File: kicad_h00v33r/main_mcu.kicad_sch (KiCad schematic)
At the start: 1 part, among them U1 STM32H723ZGT6

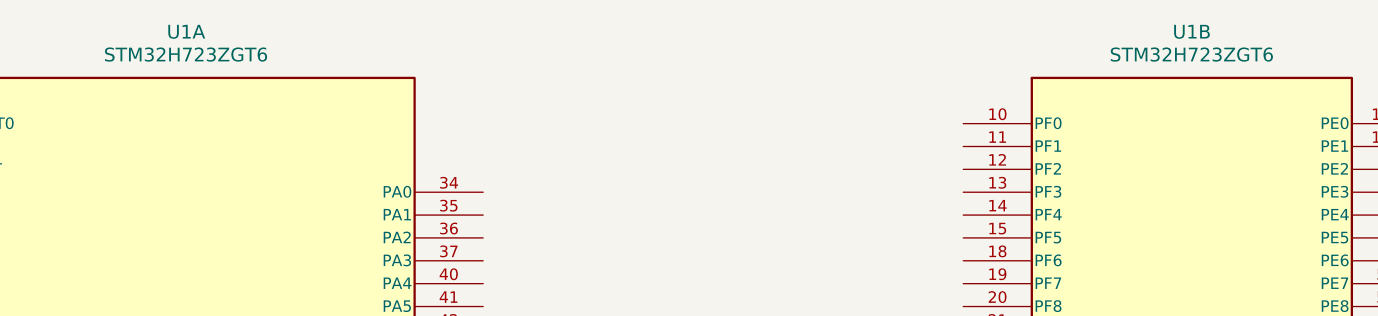
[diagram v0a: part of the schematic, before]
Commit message: power supply + HSE completed
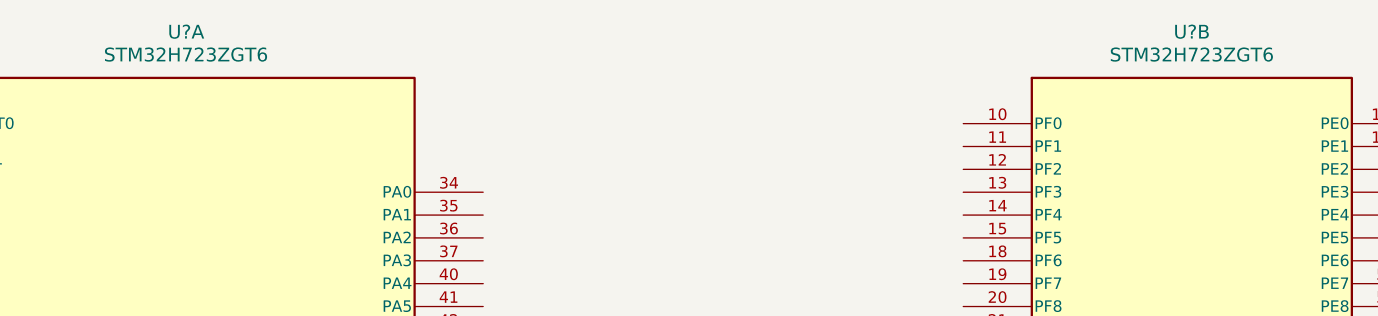
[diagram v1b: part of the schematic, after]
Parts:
- renumbered U1 to U?
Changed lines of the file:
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@@
 		(dnp no)
 		(fields_autoplaced yes)
-		(property "Reference" "U1"
+		(property "Reference" "U?"
 			(at 193.04 45.72 0)
 			(effects
@@
 			(project "kicad_h00v33r"
 				(path "/eacc50d8-8f37-499c-bdc5-63fc65cec568/4cfed190-db6f-4bff-b92a-b36a3b515167"
-					(reference "U1")
+					(reference "U?")
 					(unit 1)
 				)
@@
 		(dnp no)
 		(fields_autoplaced yes)
-		(property "Reference" "U1"
+		(property "Reference" "U?"
 			(at 304.8 45.72 0)
 			(effects
@@
 			(project "kicad_h00v33r"
 				(path "/eacc50d8-8f37-499c-bdc5-63fc65cec568/4cfed190-db6f-4bff-b92a-b36a3b515167"
-					(reference "U1")
+					(reference "U?")
 					(unit 2)
 				)
